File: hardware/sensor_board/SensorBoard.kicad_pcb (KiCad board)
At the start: 2 copper layers, 89.5 x 80 mm, 32 parts, among them J1 EXT, J10 LED L2, J11 LED L3, J12 LED R1, J13 LED R2, J14 SPARE GPIO, J15 VSYS BUS, J16 GND BUS, J17 3V3 BUS, J2 SOIL SENSOR L, J3 SOIL SENSOR R, J4 ENV SENSOR L, J5 ENV SENSOR R, J6 FEED SENSOR L, J7 FEED SENSOR R, J8 LED R3, J9 LED L1, U1 Pico, U2 74HC595

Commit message: Tidying up PCB a little bit
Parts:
- J10: value LED L2 -> LED L3
- J11: value LED L3 -> LED R1
- J12: value LED R1 -> LED R2
- J13: value LED R2 -> LED R3
- J8: value LED R3 -> LED L1
- J9: value LED L1 -> LED L2
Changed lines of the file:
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@@
       (effects (font (size 1 1) (thickness 0.15)))
     )
-    (fp_text value "LED L1" (at 6.80375 0 90) (layer "F.SilkS")
+    (fp_text value "LED L2" (at 6.80375 0 90) (layer "F.SilkS")
       (effects (font (size 1 1) (thickness 0.15)))
     )
@@
       (effects (font (size 1 1) (thickness 0.15)))
     )
-    (fp_text value "LED R1" (at 6.82375 0 270) (layer "F.SilkS")
+    (fp_text value "LED R2" (at 6.82375 0 270) (layer "F.SilkS")
       (effects (font (size 1 1) (thickness 0.15)))
     )
@@
       (effects (font (size 1 1) (thickness 0.15)))
     )
-    (fp_text value "LED R2" (at 6.82375 0 270) (layer "F.SilkS")
+    (fp_text value "LED R3" (at 6.82375 0 270) (layer "F.SilkS")
       (effects (font (size 1 1) (thickness 0.15)))
     )
@@
       (effects (font (size 1 1) (thickness 0.15)))
     )
-    (fp_text value "LED L2" (at 6.80375 0 -90) (layer "F.SilkS")
+    (fp_text value "LED L3" (at 6.80375 0 -90) (layer "F.SilkS")
       (effects (font (size 1 1) (thickness 0.15)))
     )
@@
       (effects (font (size 1 1) (thickness 0.15)))
     )
-    (fp_text value "LED R3" (at 6.82375 0 270) (layer "F.SilkS")
+    (fp_text value "LED L1" (at 6.82375 0 270) (layer "F.SilkS")
       (effects (font (size 1 1) (thickness 0.15)))
     )
@@
       (effects (font (size 1 1) (thickness 0.15)))
     )
-    (fp_text value "LED L3" (at 6.80375 0 270) (layer "F.SilkS")
+    (fp_text value "LED R1" (at 6.80375 0 270) (layer "F.SilkS")
       (effects (font (size 1 1) (thickness 0.15)))
     )
@@
   (segment (start 156.846396 73.66) (end 161.29 73.66) (width 0.25) (layer "F.Cu") (net 50))
   (segment (start 163.83 59.69) (end 171.45 59.69) (width 0.25) (layer "F.Cu") (net 50))
-  (segment (start 172.72 60.96) (end 172.72 63.5) (width 0.25) (layer "F.Cu") (net 50))
   (segment (start 162.56 60.96) (end 163.83 59.69) (width 0.25) (layer "F.Cu") (net 50))
-  (segment (start 171.45 64.77) (end 171.41 64.73) (width 0.25) (layer "F.Cu") (net 50))
-  (segment (start 172.72 63.5) (end 171.45 64.77) (width 0.25) (layer "F.Cu") (net 50))
+  (segment (start 172.72 60.96) (end 172.72 63.42) (width 0.25) (layer "F.Cu") (net 50))
   (segment (start 171.41 64.73) (end 170.18 64.73) (width 0.25) (layer "F.Cu") (net 50))
   (segment (start 161.29 73.66) (end 162.56 72.39) (width 0.25) (layer "F.Cu") (net 50))
+  (segment (start 171.41 64.73) (end 172.72 63.42) (width 0.25) (layer "F.Cu") (net 50))
   (segment (start 170.18 73.66) (end 170.18 72.23) (width 0.25) (layer "F.Cu") (net 51))
   (segment (start 169.73 74.11) (end 170.18 73.66) (width 0.25) (layer "F.Cu") (net 51))

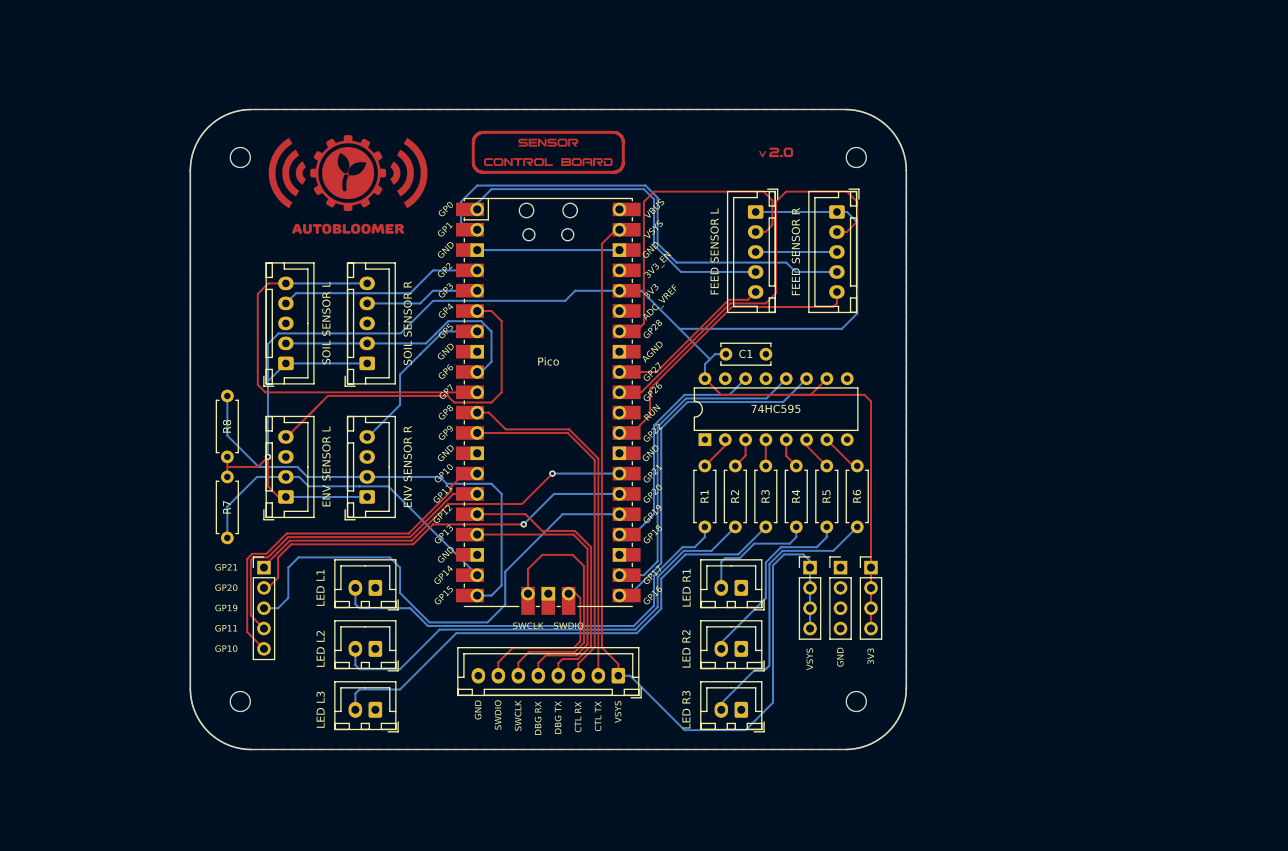
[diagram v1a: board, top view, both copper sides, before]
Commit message: Brand new sensor board, includes I2C expander, RTC and relay board connections
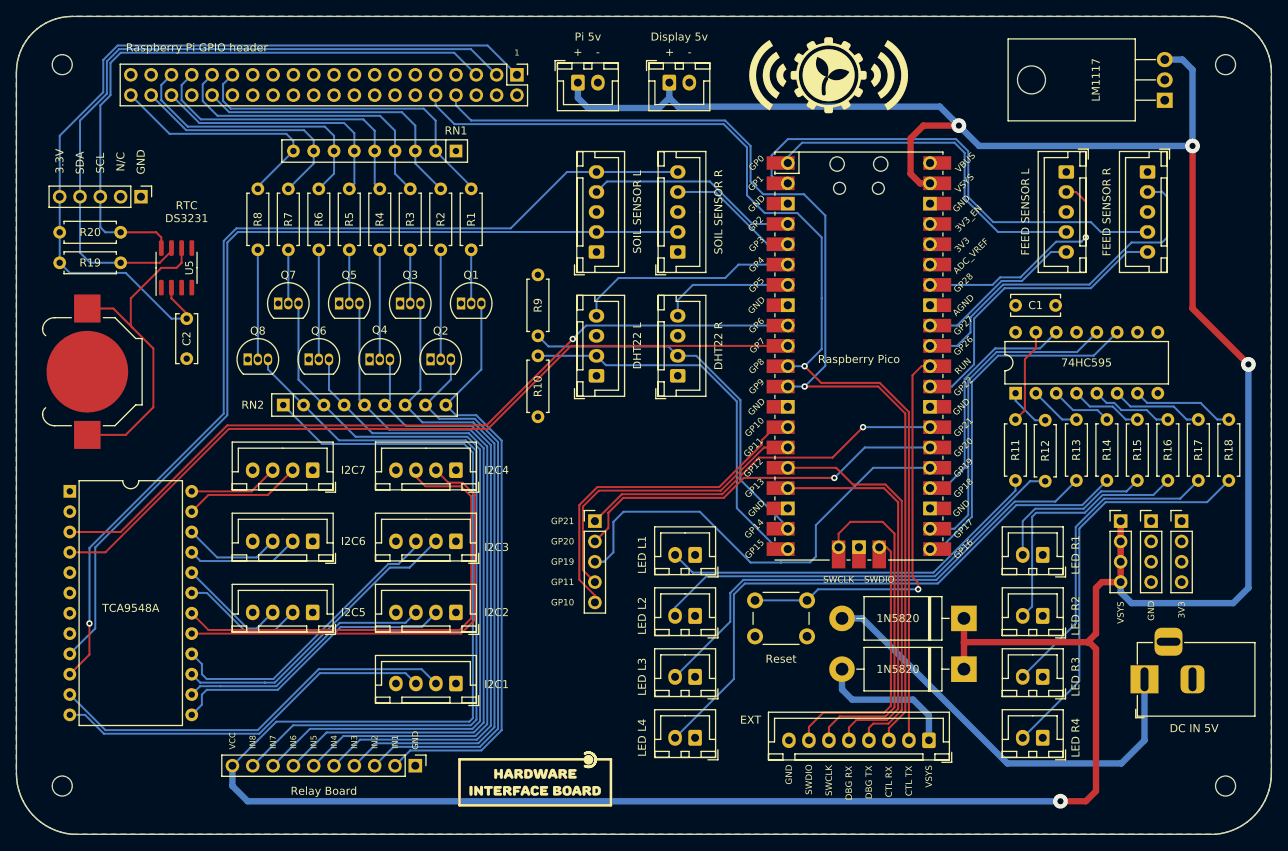
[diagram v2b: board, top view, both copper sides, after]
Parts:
- added BT1: CR1220, Battery:BatteryHolder_Keystone_3000_1x12mm, F.Cu at (76.5, 82.2)
- added C2: 0.1uf, Capacitor_THT:C_Disc_D6.0mm_W2.5mm_P5.00mm, F.Cu at (88.9, 75.6)
- added D1: 1N5820, Diode_THT:D_DO-201AD_P15.24mm_Horizontal, F.Cu at (186.1, 119.4)
- added D2: 1N5820, Diode_THT:D_DO-201AD_P15.24mm_Horizontal, F.Cu at (186.1, 113.0)
- added J1: Relay Board, Connector_PinHeader_2.54mm:PinHeader_1x10_P2.54mm_Vertical, F.Cu at (117.5, 131.4)
- added J15: LED L1, Connector_JST:JST_XH_B2B-XH-A_1x02_P2.50mm_Vertical, F.Cu at (152.5, 105.1)
- added J16: LED L2, Connector_JST:JST_XH_B2B-XH-A_1x02_P2.50mm_Vertical, F.Cu at (152.5, 112.7)
- added J2: Pi 5v, Connector_JST:JST_XH_B2B-XH-A_1x02_P2.50mm_Vertical, F.Cu at (137.8, 46.1)
- added J24: Raspberry Pi GPIO header, Connector_PinHeader_2.54mm:PinHeader_2x20_P2.54mm_Vertical, F.Cu at (130.2, 45.1)
- added J25: RTC Header, Connector_PinHeader_2.54mm:PinHeader_1x05_P2.54mm_Vertical, F.Cu at (83.2, 60.3)
- added J26: I2C3, Connector_JST:JST_XH_B4B-XH-A_1x04_P2.50mm_Vertical, F.Cu at (122.6, 103.4)
- added J27: I2C2, Connector_JST:JST_XH_B4B-XH-A_1x04_P2.50mm_Vertical, F.Cu at (122.6, 112.3)
- added J28: I2C1, Connector_JST:JST_XH_B4B-XH-A_1x04_P2.50mm_Vertical, F.Cu at (122.6, 121.2)
- added J29: I2C4, Connector_JST:JST_XH_B4B-XH-A_1x04_P2.50mm_Vertical, F.Cu at (122.6, 94.5)
- added J3: Display 5v, Connector_JST:JST_XH_B2B-XH-A_1x02_P2.50mm_Vertical, F.Cu at (149.2, 46.1)
- added J30: I2C5, Connector_JST:JST_XH_B4B-XH-A_1x04_P2.50mm_Vertical, F.Cu at (104.7, 112.3)
- added J31: I2C6, Connector_JST:JST_XH_B4B-XH-A_1x04_P2.50mm_Vertical, F.Cu at (104.7, 103.4)
- added J32: I2C7, Connector_JST:JST_XH_B4B-XH-A_1x04_P2.50mm_Vertical, F.Cu at (104.7, 94.5)
- added J4: DC IN 5V, Connector_BarrelJack:BarrelJack_Horizontal, F.Cu at (208.6, 120.7)
- added Q1: PN2222A, Package_TO_SOT_THT:TO-92_Inline, F.Cu at (123.2, 73.7)
- added Q2: PN2222A, Package_TO_SOT_THT:TO-92_Inline, F.Cu at (119.4, 80.7)
- added Q3: PN2222A, Package_TO_SOT_THT:TO-92_Inline, F.Cu at (115.6, 73.7)
- added Q4: PN2222A, Package_TO_SOT_THT:TO-92_Inline, F.Cu at (111.8, 80.7)
- added Q5: PN2222A, Package_TO_SOT_THT:TO-92_Inline, F.Cu at (108.0, 73.7)
- added Q6: PN2222A, Package_TO_SOT_THT:TO-92_Inline, F.Cu at (104.1, 80.7)
- added Q7: PN2222A, Package_TO_SOT_THT:TO-92_Inline, F.Cu at (100.3, 73.7)
- added Q8: PN2222A, Package_TO_SOT_THT:TO-92_Inline, F.Cu at (96.5, 80.7)
- added R1: 2.2k, Resistor_THT:R_Axial_DIN0207_L6.3mm_D2.5mm_P7.62mm_Horizontal, F.Cu at (124.5, 59.3)
- added R11: R1, Resistor_THT:R_Axial_DIN0207_L6.3mm_D2.5mm_P7.62mm_Horizontal, F.Cu at (192.5, 88.2)
- added R12: R1, Resistor_THT:R_Axial_DIN0207_L6.3mm_D2.5mm_P7.62mm_Horizontal, F.Cu at (196.2, 88.3)
- added R19: 4.3k, Resistor_THT:R_Axial_DIN0207_L6.3mm_D2.5mm_P7.62mm_Horizontal, F.Cu at (73.0, 68.6)
- added R2: 2.2k, Resistor_THT:R_Axial_DIN0207_L6.3mm_D2.5mm_P7.62mm_Horizontal, F.Cu at (120.7, 59.3)
- added R20: 4.3k, Resistor_THT:R_Axial_DIN0207_L6.3mm_D2.5mm_P7.62mm_Horizontal, F.Cu at (73.0, 64.8)
- added R3: 2.2k, Resistor_THT:R_Axial_DIN0207_L6.3mm_D2.5mm_P7.62mm_Horizontal, F.Cu at (116.8, 59.3)
- added R4: 2.2k, Resistor_THT:R_Axial_DIN0207_L6.3mm_D2.5mm_P7.62mm_Horizontal, F.Cu at (113.0, 59.3)
- added R5: 2.2k, Resistor_THT:R_Axial_DIN0207_L6.3mm_D2.5mm_P7.62mm_Horizontal, F.Cu at (109.2, 59.3)
- added R6: 2.2k, Resistor_THT:R_Axial_DIN0207_L6.3mm_D2.5mm_P7.62mm_Horizontal, F.Cu at (105.4, 59.3)
- added R7: 2.2k, Resistor_THT:R_Axial_DIN0207_L6.3mm_D2.5mm_P7.62mm_Horizontal, F.Cu at (101.6, 59.3)
- added R8: 2.2k, Resistor_THT:R_Axial_DIN0207_L6.3mm_D2.5mm_P7.62mm_Horizontal, F.Cu at (97.8, 59.3)
- added RN1: 10k, Resistor_THT:R_Array_SIP9, F.Cu at (122.6, 54.6)
- added RN2: 10k, Resistor_THT:R_Array_SIP9, F.Cu at (101.0, 86.4)
- added SW1: Reset, Button_Switch_THT:SW_PUSH_6mm, F.Cu at (166.4, 115.3)
- added U3: TCA9548A, Package_DIP:DIP-24_W15.24mm, F.Cu at (74.3, 97.2)
- added U4: LM1117, Package_TO_SOT_THT:TO-220-3_Horizontal_TabDown, F.Cu at (211.2, 48.3)
- added U5: DS3231MZ, Package_SO:SOIC-8_3.9x4.9mm_P1.27mm, F.Cu at (87.6, 69.2)
- J12: renamed from J4; value ENV SENSOR L -> DHT22 R
- J14: renamed from J5; value ENV SENSOR R -> DHT22 L
- J17: renamed from J8; value LED L1 -> LED L3
- J18: renamed from J9; value LED L2 -> LED L4
- J19: renamed from J10; value LED L3 -> LED R1
- J21: renamed from J11; value LED R1 -> LED R2
- J22: renamed from J12; value LED R2 -> LED R3
- J23: renamed from J13; value LED R3 -> LED R4
- U1: value Pico -> Raspberry Pico
- moved J19 85.6 mm to (195.9, 105.1)
- moved J12 51.3 mm to (150.3, 82.7)
- moved H3 47.6 mm to (218.8, 43.8)
- moved H4 47.3 mm to (218.8, 134.0)
- moved R13 46.8 mm to (200.1, 88.2)
- moved R14 46.8 mm to (203.9, 88.2)
- moved R15 46.8 mm to (207.7, 88.2)
- moved R16 46.8 mm to (211.5, 88.2)
- moved R17 46.8 mm to (215.4, 88.2)
- moved R18 46.8 mm to (219.2, 88.2)
- moved R9 46.3 mm to (132.8, 77.7)
- moved J13 41.8 mm to (139.9, 100.9)
- moved J17 41.5 mm to (152.5, 120.3)
- moved J18 41.5 mm to (152.5, 128.0)
- moved J6 41.2 mm to (140.1, 67.2)
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- renumbered J16 to J10, J7 to J11, J14 to J13, J1 to J20, J15 to J5, J2 to J6, J17 to J7, J6 to J8, J3 to J9, R8 to R10, R1 to R13, R2 to R14, R3 to R15, R4 to R16, R5 to R17, R6 to R18, R7 to R9
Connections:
- J12 pad 2: /ENV SENSOR L CTL -> /ENV SENSOR R CTL
- J12 pad 4: /ENV SENSOR L DETECT -> /DHT22 R DETECT
- J14 pad 2: /ENV SENSOR R CTL -> /ENV SENSOR L CTL
- J14 pad 4: /ENV SENSOR R DETECT -> /DHT22 L DETECT
- J20 pad 1: VS -> /VSYS
- J6 pad 2: /I2C1 SDA -> Net-(J6-Pad2)
- J6 pad 5: /I2C1 SCL -> Net-(J6-Pad5)
- J9 pad 2: /I2C1 SDA -> Net-(J6-Pad2)
- J9 pad 5: /I2C1 SCL -> Net-(J6-Pad5)
- R10 pad 1: /ENV SENSOR R CTL -> /ENV SENSOR L CTL
- R9 pad 1: /ENV SENSOR L CTL -> /ENV SENSOR R CTL
- U1 pad 19: /ENV SENSOR L CTL -> /ENV SENSOR R CTL
- U1 pad 20: /ENV SENSOR R CTL -> /ENV SENSOR L CTL
- U1 pad 30: unconnected-(U1-Pad30) -> Net-(SW1-Pad2)
- U1 pad 36: +3V3 -> unconnected-(U1-Pad36)
- U1 pad 6: /ENV SENSOR L DETECT -> /DHT22 L DETECT
- U1 pad 7: /ENV SENSOR R DETECT -> /DHT22 R DETECT
- U2 pad 1: unconnected-(U2-Pad1) -> Net-(R12-Pad1)
- U2 pad 15: unconnected-(U2-Pad15) -> Net-(R11-Pad1)
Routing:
- net VS: track 112.0 -> 451.4 mm, vias 0 -> 4
- net +3V3: track 222.5 -> 0.00 mm, vias 1 -> 0
- net Net-(J6-Pad5): track 0.00 -> 122.5 mm, vias 0 -> 1
- net Net-(J6-Pad2): track 0.00 -> 116.4 mm
- net Net-(C2-Pad1): track 0.00 -> 104.4 mm
- net Net-(J1-Pad8): track 0.00 -> 98.0 mm
- net Net-(J1-Pad9): track 0.00 -> 95.5 mm
- net /CTL RX: track 43.9 -> 136.0 mm, vias 0 -> 1
- net /CTL TX: track 44.7 -> 135.4 mm, vias 0 -> 1
- net Net-(J1-Pad6): track 0.00 -> 88.6 mm
- net Net-(J24-Pad3): track 0.00 -> 88.5 mm
- net Net-(J1-Pad7): track 0.00 -> 86.1 mm
- net Net-(J1-Pad4): track 0.00 -> 81.2 mm
- net Net-(J24-Pad5): track 0.00 -> 77.9 mm
- net Net-(J1-Pad5): track 0.00 -> 77.7 mm
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- added copper zone on B.Cu, net +3V3
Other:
- board size 89.5 x 80 mm -> 156.9 x 102.2 mm
- board text added: "+"
- board text added: "-"
- board text added: "1"
- board text added: "3.3V"
- board text added: "IN1"
- board text added: "IN2"
- board text added: "IN3"
- board text added: "IN4"
- board text added: "IN5"
- board text added: "IN6"
- board text added: "IN7"
- board text added: "IN8"
- board text added: "N/C"
- board text added: "RTC DS3231"
- board text added: "SCL"
- board text added: "SDA"
- board text added: "VCC"
- board text added: "© AutoBloomer.com 2023"
- board text removed: "© AutoBloomer.com 2022"

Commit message: New version without DHT22. Full exposed I2C expander
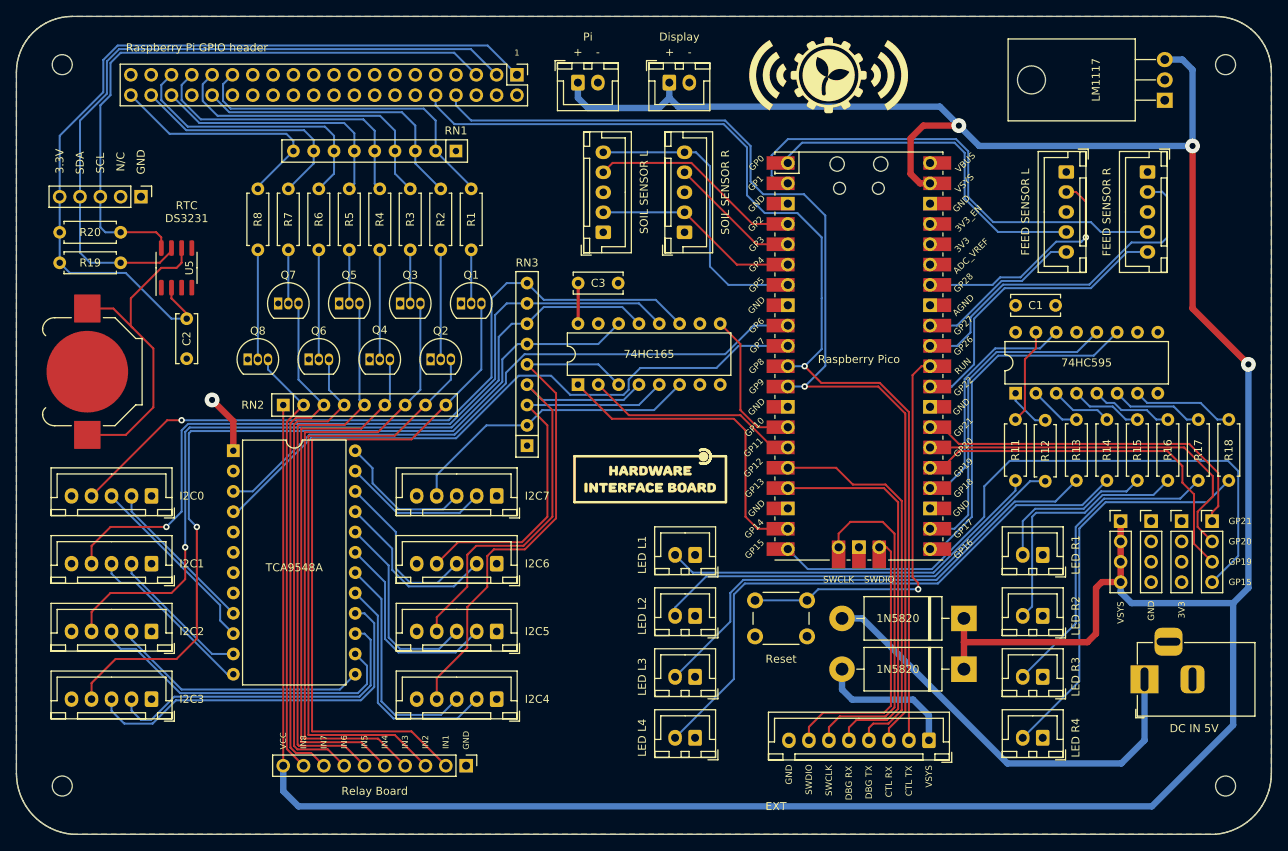
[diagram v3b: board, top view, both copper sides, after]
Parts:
- removed J12: DHT22 R, Connector_JST:JST_XH_B4B-XH-A_1x04_P2.50mm_Vertical
- removed J14: DHT22 L, Connector_JST:JST_XH_B4B-XH-A_1x04_P2.50mm_Vertical
- removed R10: R8, Resistor_THT:R_Axial_DIN0207_L6.3mm_D2.5mm_P7.62mm_Horizontal
- removed R9: R7, Resistor_THT:R_Axial_DIN0207_L6.3mm_D2.5mm_P7.62mm_Horizontal
- added C3: 0.1uf, Capacitor_THT:C_Disc_D6.0mm_W2.5mm_P5.00mm, F.Cu at (137.8, 71.1)
- added J26: I2C0, Connector_JST:JST_XH_B5B-XH-A_1x05_P2.50mm_Vertical, F.Cu at (84.5, 97.7)
- added RN3: 10k, Resistor_THT:R_Array_SIP9, F.Cu at (131.4, 91.4)
- added U6: 74HC165, Package_DIP:DIP-16_W7.62mm, F.Cu at (137.8, 83.8)
- J13: footprint Connector_PinHeader_2.54mm:PinHeader_1x05_P2.54mm_Vertical -> Connector_PinHeader_2.54mm:PinHeader_1x04_P2.54mm_Vertical
- J2: value Pi 5v -> Pi
- J27: renamed from J28; footprint Connector_JST:JST_XH_B4B-XH-A_1x04_P2.50mm_Vertical -> Connector_JST:JST_XH_B5B-XH-A_1x05_P2.50mm_Vertical
- J28: renamed from J27; footprint Connector_JST:JST_XH_B4B-XH-A_1x04_P2.50mm_Vertical -> Connector_JST:JST_XH_B5B-XH-A_1x05_P2.50mm_Vertical
- J29: renamed from J26; footprint Connector_JST:JST_XH_B4B-XH-A_1x04_P2.50mm_Vertical -> Connector_JST:JST_XH_B5B-XH-A_1x05_P2.50mm_Vertical
- J3: value Display 5v -> Display
- J30: renamed from J29; footprint Connector_JST:JST_XH_B4B-XH-A_1x04_P2.50mm_Vertical -> Connector_JST:JST_XH_B5B-XH-A_1x05_P2.50mm_Vertical
- J31: renamed from J30; footprint Connector_JST:JST_XH_B4B-XH-A_1x04_P2.50mm_Vertical -> Connector_JST:JST_XH_B5B-XH-A_1x05_P2.50mm_Vertical
- J32: renamed from J31; footprint Connector_JST:JST_XH_B4B-XH-A_1x04_P2.50mm_Vertical -> Connector_JST:JST_XH_B5B-XH-A_1x05_P2.50mm_Vertical
- J33: renamed from J32; footprint Connector_JST:JST_XH_B4B-XH-A_1x04_P2.50mm_Vertical -> Connector_JST:JST_XH_B5B-XH-A_1x05_P2.50mm_Vertical
- moved J13 77.1 mm to (217.1, 100.9)
- moved J29 42.9 mm to (84.5, 123.1)
- moved J27 40.9 mm to (84.5, 106.2)
- moved J28 38.1 mm to (84.5, 114.7)
- moved J30 29.1 mm to (127.7, 123.1)
- moved J33 23.2 mm to (127.7, 97.7)
- moved J32 23.2 mm to (127.7, 106.2)
- moved J31 23.1 mm to (127.7, 114.7)
- moved U3 21.1 mm to (94.7, 92.1)
- moved J1 6.35 mm to (123.8, 131.4)
- moved J6 2.60 mm to (141.0, 64.8)
- moved J9 2.60 mm to (151.1, 64.8)
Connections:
- J13 pad 4: /GPIO11 -> /GPIO15
- J27 pad 4: GND -> Net-(J27-Pad4)
- J28 pad 4: GND -> Net-(J28-Pad4)
- J29 pad 4: GND -> Net-(J29-Pad4)
- J30 pad 4: GND -> Net-(J30-Pad4)
- J31 pad 4: GND -> Net-(J31-Pad4)
- J32 pad 4: GND -> Net-(J32-Pad4)
- J33 pad 4: GND -> Net-(J33-Pad4)
- J6 pad 2: Net-(J6-Pad2) -> Net-(U1-Pad6)
- J6 pad 5: Net-(J6-Pad5) -> Net-(U1-Pad7)
- J9 pad 2: Net-(J6-Pad2) -> Net-(U1-Pad6)
- J9 pad 5: Net-(J6-Pad5) -> Net-(U1-Pad7)
- U1 pad 14: /GPIO10 -> Net-(U1-Pad14)
- U1 pad 15: /GPIO11 -> Net-(U1-Pad15)
- U1 pad 19: /ENV SENSOR R CTL -> Net-(U1-Pad19)
- U1 pad 20: /ENV SENSOR L CTL -> /GPIO15
- U1 pad 6: /DHT22 L DETECT -> Net-(U1-Pad6)
- U1 pad 7: /DHT22 R DETECT -> Net-(U1-Pad7)
- U3 pad 10: Net-(J6-Pad5) -> Net-(J26-Pad3)
- U3 pad 9: Net-(J6-Pad2) -> Net-(J26-Pad2)
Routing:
- net Net-(J6-Pad5): track 122.5 -> 0.00 mm, vias 1 -> 0
- net Net-(J6-Pad2): track 116.4 -> 0.00 mm
- net Net-(J29-Pad4): track 0.00 -> 104.6 mm, vias 0 -> 1
- net Net-(J28-Pad4): track 0.00 -> 101.3 mm, vias 0 -> 1
- net Net-(J27-Pad4): track 0.00 -> 97.4 mm, vias 0 -> 1
- net Net-(J26-Pad4): track 0.00 -> 92.4 mm, vias 0 -> 1
- net /GPIO15: track 0.00 -> 80.9 mm
- net Net-(J30-Pad4): track 0.00 -> 64.3 mm
- net Net-(J31-Pad4): track 0.00 -> 57.2 mm
- net /ENV SENSOR L CTL: track 49.1 -> 0.00 mm
- net Net-(J32-Pad4): track 0.00 -> 48.9 mm
- net /ENV SENSOR R CTL: track 47.0 -> 0.00 mm
- net /GPIO10: track 41.8 -> 0.00 mm
- net Net-(J1-Pad9): track 95.5 -> 54.4 mm
- net Net-(U1-Pad19): track 0.00 -> 40.0 mm
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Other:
- board text added: "GP15"
- board text removed: "GP10"
- board text removed: "GP11"
